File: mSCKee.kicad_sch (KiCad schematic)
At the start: 1 part

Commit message: chore: Reinit and readd RP2040 minimal circuit
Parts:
- removed U?: RP2040, Package_DFN_QFN:QFN-56-1EP_7x7mm_P0.4mm_EP3.2x3.2mm, symbol MCU_RaspberryPi:RP2040
- added C1, C17, C4: 10u, Capacitor_SMD:C_0805_2012Metric, symbol Device:C
- added C10, C8: 1u, Capacitor_SMD:C_0402_1005Metric, symbol Device:C
- added C11, C12, C13, C14, C15, C16, C5, C6, C7, C9: 100n, Capacitor_SMD:C_0402_1005Metric, symbol Device:C
- added C2, C3: 15p, Capacitor_SMD:C_0402_1005Metric, symbol Device:C
- added H1, H2, H3, H4: MountingHole, MountingHole:MountingHole_2.7mm_M2.5, symbol Mechanical:MountingHole
- added J1: USB_B_Micro, RP2040_minimal:USB_Micro-B_Amphenol_10103594-0001LF_Horizontal_modified, symbol Connector:USB_B_Micro
- added J2: Conn_01x02, Connector_PinHeader_2.54mm:PinHeader_1x02_P2.54mm_Vertical, symbol Connector_Generic:Conn_01x02
- added J3, J4: Conn_02x18_Odd_Even, Connector_PinHeader_2.54mm:PinHeader_2x18_P2.54mm_Vertical, symbol Connector_Generic:Conn_02x18_Odd_Even
- added R1, R5: 1k, Resistor_SMD:R_0402_1005Metric, symbol Device:R
- added R2: DNF, Resistor_SMD:R_0402_1005Metric, symbol Device:R
- added R3, R4: 27, Resistor_SMD:R_0402_1005Metric, symbol Device:R
- added U1: NCP1117-3.3_SOT223, Package_TO_SOT_SMD:SOT-223-3_TabPin2, symbol Regulator_Linear:NCP1117-3.3_SOT223
- added U2: W25Q128JVS, Package_SO:SOIC-8_5.23x5.23mm_P1.27mm, symbol Memory_Flash:W25Q128JVS
- added U3: RP2040, RP2040_minimal:RP2040-QFN-56, symbol MCU_RaspberryPi_RP2040:RP2040
- added Y1: ABM8-272-T3, Crystal:Crystal_SMD_3225-4Pin_3.2x2.5mm, symbol Device:Crystal_GND24
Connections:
- new net: R4.2, U3.46 (USB_DM)
- new net: R3.2, U3.47 (USB_DP)
- new net: C3.1, R5.2, Y1.3
- new net +1V1: C6.1, C7.1, C8.1, U3.23 (DVDD), U3.45 (VREG_VOUT), U3.50 (DVDD)
- new net +3V3: C10.1, C11.1, C12.1, C13.1, C14.1, C15.1, C16.1, C17.1, C4.1, C5.1, C9.1, J3.2 (Pin_2), R2.1, U1.2 (VO), U2.8 (VCC), U3.1 (IOVDD), U3.10 (IOVDD), U3.22 (IOVDD), U3.33 (IOVDD), U3.42 (IOVDD), U3.43 (ADC_AVDD), U3.44 (VREG_IN), U3.48 (USB_VDD), U3.49 (IOVDD)
- new net GND: C1.2, C10.2, C11.2, C12.2, C13.2, C14.2, C15.2, C16.2, C17.2, C2.2, C3.2, C4.2, C5.2, C6.2, C7.2, C8.2, C9.2, J1.5 (GND), J1.6 (Shield), J2.2 (Pin_2), J3.1 (Pin_1), J3.11 (Pin_11), J3.13 (Pin_13), J3.15 (Pin_15), J3.17 (Pin_17), J3.19 (Pin_19), J3.21 (Pin_21), J3.23 (Pin_23), J3.25 (Pin_25), J3.27 (Pin_27), J3.29 (Pin_29), J3.3 (Pin_3), J3.31 (Pin_31), J3.33 (Pin_33), J3.35 (Pin_35), J3.36 (Pin_36), J3.5 (Pin_5), J3.7 (Pin_7), J3.9 (Pin_9), J4.10 (Pin_10), J4.12 (Pin_12), J4.14 (Pin_14), J4.16 (Pin_16), J4.18 (Pin_18), J4.2 (Pin_2), J4.20 (Pin_20), J4.22 (Pin_22), J4.24 (Pin_24), J4.26 (Pin_26), J4.28 (Pin_28), J4.30 (Pin_30), J4.32 (Pin_32), J4.34 (Pin_34), J4.35 (Pin_35), J4.36 (Pin_36), J4.4 (Pin_4), J4.6 (Pin_6), J4.8 (Pin_8), U1.1 (GND), U2.4 (GND), U3.19 (TESTEN), U3.57 (GND), Y1.2, Y1.4
- new net GPIO0: J3.4 (Pin_4)
- new net GPIO1: J3.6 (Pin_6)
- new net GPIO10: J3.24 (Pin_24)
- new net GPIO11: J3.26 (Pin_26)
- new net GPIO12: J3.28 (Pin_28)
- new net GPIO13: J3.30 (Pin_30)
- new net GPIO14: J3.32 (Pin_32)
- new net GPIO15: J3.34 (Pin_34)
- new net GPIO16: J4.27 (Pin_27)
- new net GPIO17: J4.25 (Pin_25)
- new net GPIO18: J4.23 (Pin_23)
- new net GPIO19: J4.21 (Pin_21)
- new net GPIO2: J3.8 (Pin_8)
- new net GPIO20: J4.19 (Pin_19)
- new net GPIO21: J4.17 (Pin_17)
- new net GPIO22: J4.15 (Pin_15)
- new net GPIO23: J4.13 (Pin_13)
- new net GPIO24: J4.11 (Pin_11)
- new net GPIO25: J4.9 (Pin_9)
- new net GPIO26_ADC0: J4.7 (Pin_7)
- new net GPIO27_ADC1: J4.5 (Pin_5)
- new net GPIO28_ADC2: J4.3 (Pin_3)
- new net GPIO29_ADC3: J4.1 (Pin_1)
- new net GPIO3: J3.10 (Pin_10)
- new net GPIO4: J3.12 (Pin_12)
- new net GPIO5: J3.14 (Pin_14)
- new net GPIO6: J3.16 (Pin_16)
- new net GPIO7: J3.18 (Pin_18)
- new net GPIO8: J3.20 (Pin_20)
- new net GPIO9: J3.22 (Pin_22)
- new net QSPI_SCLK: U2.6 (CLK)
- new net QSPI_SD0: U2.5 (DI(IO0))
- new net QSPI_SD1: U2.2 (DO(IO1))
- new net QSPI_SD2: U2.3 (IO2)
- new net QSPI_SD3: U2.7 (IO3)
- new net QSPI_SS: R1.1, R2.2, U2.1 (~{CS})
- new net RUN: J4.29 (Pin_29)
- new net SWCLK: J4.33 (Pin_33)
- new net SWD: J4.31 (Pin_31)
- new net USB_D+: J1.3 (D+), R3.1
- new net USB_D-: J1.2 (D-), R4.1
- new net VBUS: C1.1, J1.1 (VBUS), U1.3 (VI)
- new net XIN: C2.1, U3.20 (XIN), Y1.1
- new net XOUT: R5.1, U3.21 (XOUT)
- new net ~{USB_BOOT}: J2.1 (Pin_1), R1.2
- no-connect marks 0 -> 1
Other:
- note added: "Crystal"
- note added: "Flash"
- note added: "IOs"
- note added: "Make sure C10 is close to pin 44 of RP2040"
- note added: "Make sure C8 is close to pin 45 of RP2040"
- note added: "Make sure R3 and R4 are close to RP2040"
- note added: "Power"

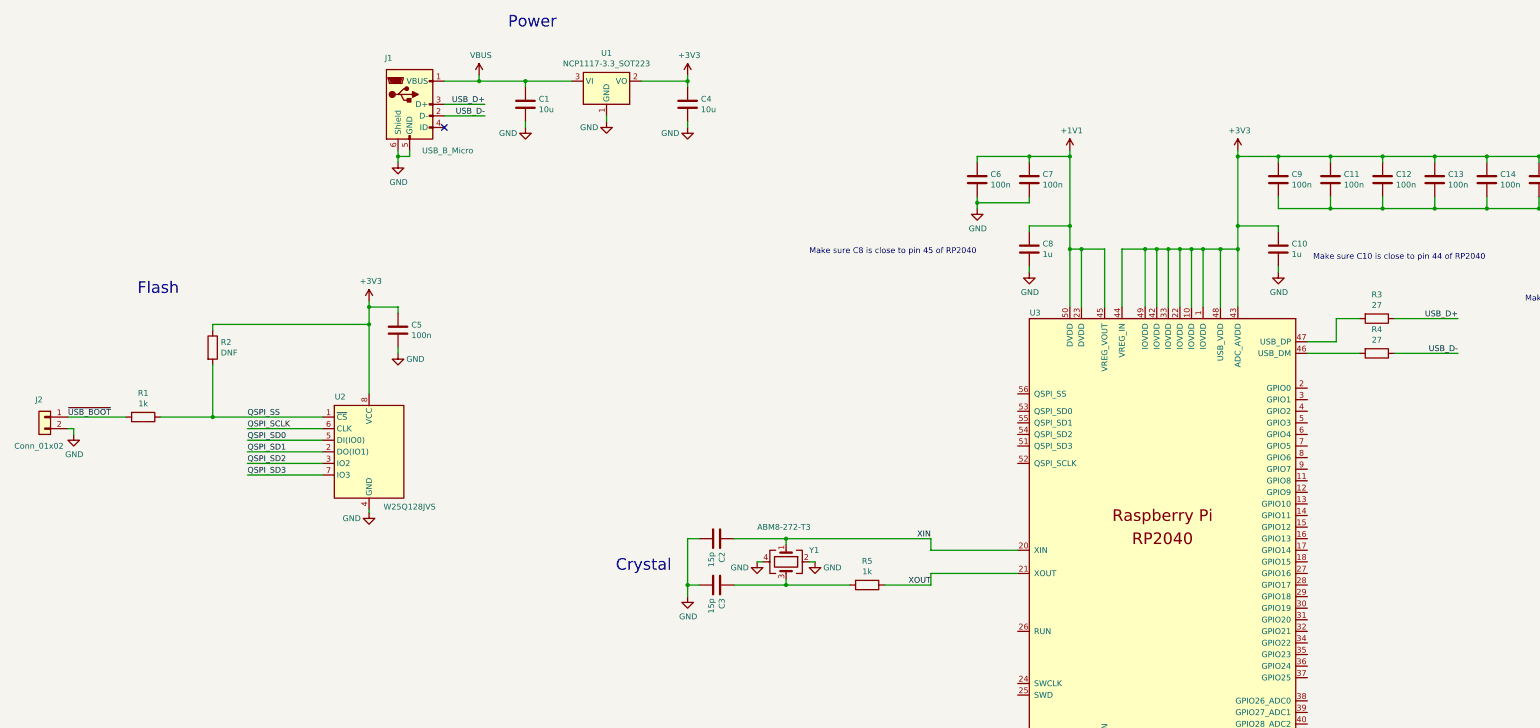
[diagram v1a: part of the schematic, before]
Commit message: feat(schematic): Connect crystal and flash chip to RP2040
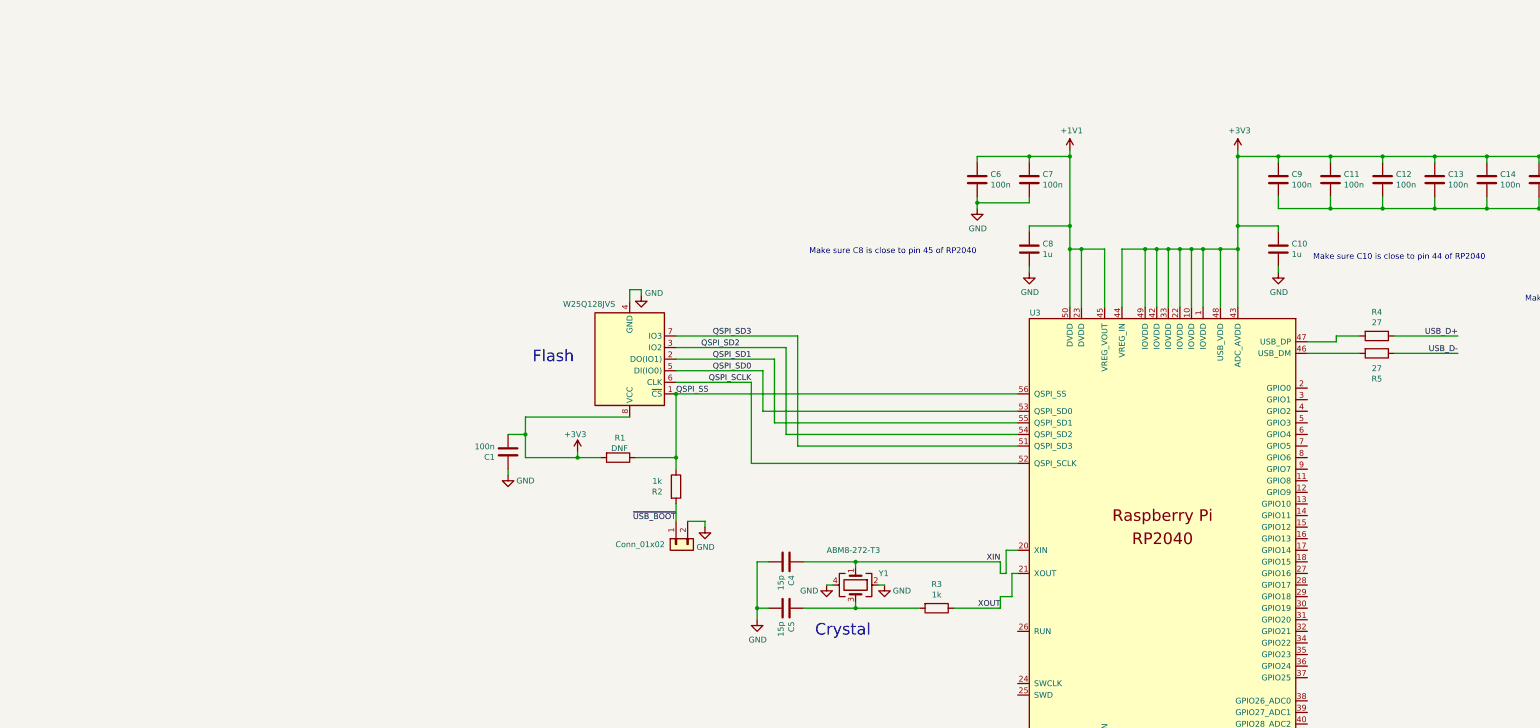
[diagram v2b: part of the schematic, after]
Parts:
- removed C1, C4: 10u, Capacitor_SMD:C_0805_2012Metric, symbol Device:C
- removed J1: USB_B_Micro, RP2040_minimal:USB_Micro-B_Amphenol_10103594-0001LF_Horizontal_modified, symbol Connector:USB_B_Micro
- removed U1: NCP1117-3.3_SOT223, Package_TO_SOT_SMD:SOT-223-3_TabPin2, symbol Regulator_Linear:NCP1117-3.3_SOT223
- removed U2: W25Q128JVS, Package_SO:SOIC-8_5.23x5.23mm_P1.27mm, symbol Memory_Flash:W25Q128JVS
- added U1: W25Q128JVS, W25Q128JVSIQ:SOIC127P790X216-8N, symbol library:W25Q128JVS
- C1: renamed from C5; symbol Device:C -> library:C
- C10, C11, C12, C13, C14, C15, C16, C17, C6, C7, C8, C9: symbol Device:C -> library:C
- C4: renamed from C2; symbol Device:C -> library:C
- C5: renamed from C3; symbol Device:C -> library:C
- H1, H2, H3, H4: symbol Mechanical:MountingHole -> library:MountingHole
- J2: symbol Connector_Generic:Conn_01x02 -> library:Conn_01x02
- J3, J4: symbol Connector_Generic:Conn_02x18_Odd_Even -> library:Conn_02x18_Odd_Even
- R1: renamed from R2; symbol Device:R -> library:R
- R2: renamed from R1; symbol Device:R -> library:R
- R3: renamed from R5; symbol Device:R -> library:R
- R4: renamed from R3; symbol Device:R -> library:R
- R5: renamed from R4; symbol Device:R -> library:R
- U3: footprint RP2040_minimal:RP2040-QFN-56 -> Package_DFN_QFN:QFN-56-1EP_7x7mm_P0.4mm_EP3.2x3.2mm; symbol MCU_RaspberryPi_RP2040:RP2040 -> library:RP2040
- Y1: symbol Device:Crystal_GND24 -> library:Crystal_GND24
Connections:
- net +3V3: now also C1.2, R1.2, U1.8 (VCC); no longer C1.1, R1.1
- net GND: now also C1.1, U1.4 (GND); no longer C1.2
- net QSPI_SCLK: now also U3.52 (QSPI_SCLK), U1.6 (CLK)
- net QSPI_SD0: now also U3.53 (QSPI_SD0), U1.5 (DI(IO0))
- net QSPI_SD1: now also U3.55 (QSPI_SD1), U1.2 (DO(IO1))
- net QSPI_SD2: now also U3.54 (QSPI_SD2), U1.3 (IO2)
- net QSPI_SD3: now also U3.51 (QSPI_SD3), U1.7 (IO3)
- net QSPI_SS: now also R1.1, U3.56 (QSPI_SS), U1.1 (~{CS}); no longer R1.2
- no-connect marks 1 -> 0
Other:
- note removed: "Power"
- moved on the sheet: C1, C4, C5, R1, R2, R3, R4, Y1

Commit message: feat(schematic): Wire up USB-C receptacle
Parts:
- added C2, C3: 10u, Capacitor_SMD:C_0805_2012Metric, symbol Device:C
- added J5: USB_C_Receptacle_USB2.0_14P, symbol Connector:USB_C_Receptacle_USB2.0_14P
- added R6, R7: 5.1k, symbol library:R
- added TP1, TP2: TestPoint, symbol Connector:TestPoint
- added U2: NCP1117-3.3_SOT223, Package_TO_SOT_SMD:SOT-223-3_TabPin2, symbol Regulator_Linear:NCP1117-3.3_SOT223
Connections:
- net +3V3: now also C3.1, U2.2 (VO)
- net GND: now also C2.2, C3.2, J5.A1 (GND), J5.A12 (GND), J5.B1 (GND), J5.B12 (GND), J5.S1 (SHIELD), R6.1, R7.1, TP2.1, U2.1 (GND)
- net USB_D+: now also J5.A6 (D+), J5.B6 (D+)
- net USB_D-: now also J5.A7 (D-), J5.B7 (D-)
- net +1V1: no longer names the net of C6.1, C7.1, C8.1, U3.23 (DVDD), U3.45 (VREG_VOUT), U3.50 (DVDD)
- new net: C2.1, J5.A4 (VBUS), J5.A9 (VBUS), J5.B4 (VBUS), J5.B9 (VBUS), TP1.1, U2.3 (VI)
- new net: J5.B5 (CC2), R6.2
- new net: J5.A5 (CC1), R7.2
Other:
- note added: "Power"
- title: (none) -> mSCKee - Split Keyboard
- moved on the sheet: C11, C12, C13, C14, C15, C16, C17, C4, C5, C9, J3, J4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

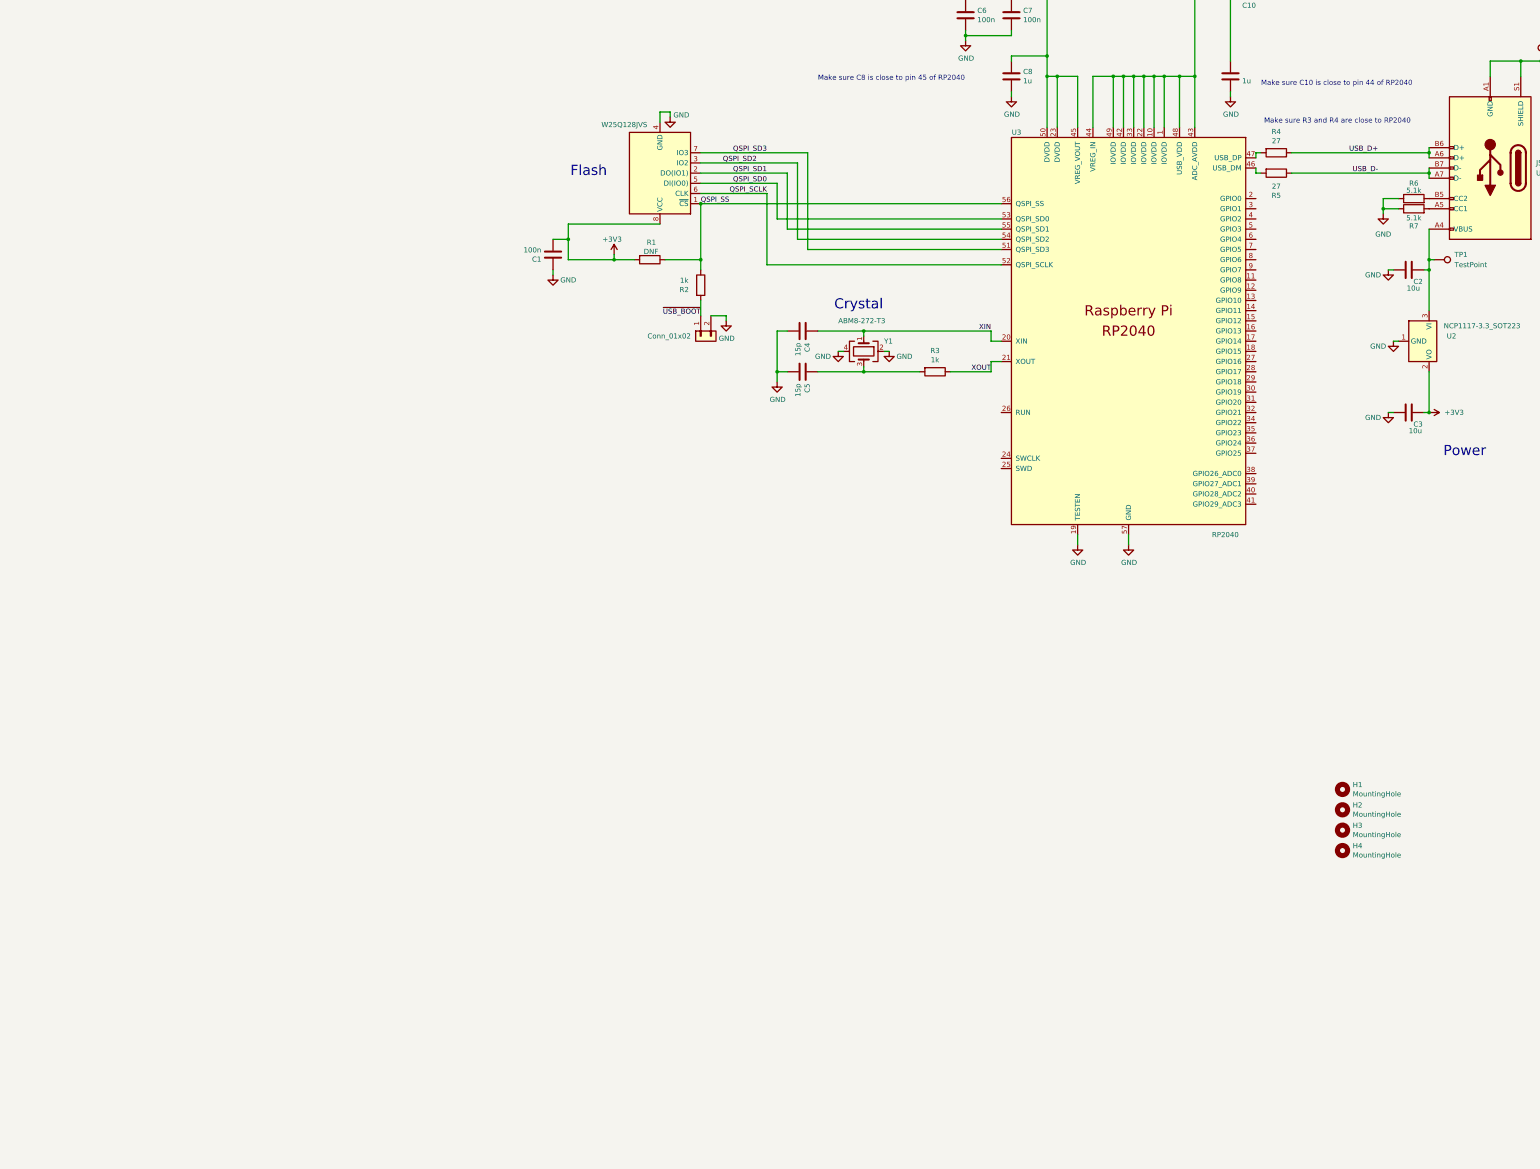
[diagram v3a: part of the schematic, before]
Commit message: feat(schematic): Add GPIO connection labels and an LED to one
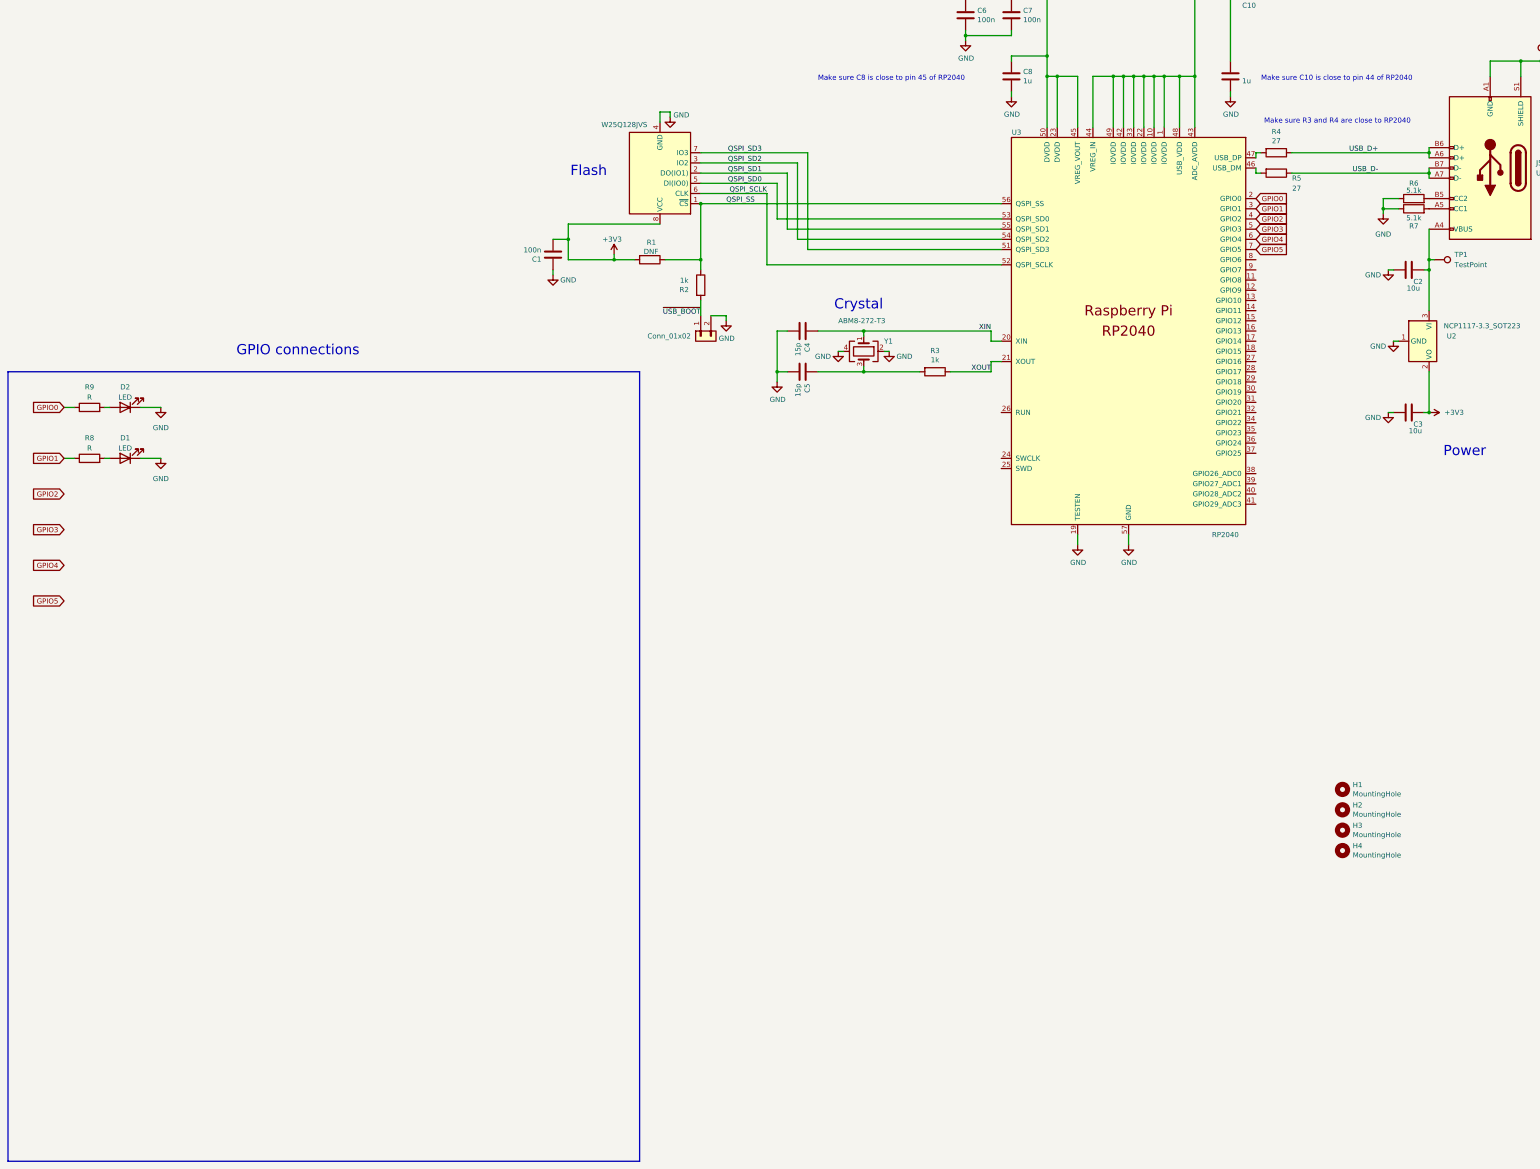
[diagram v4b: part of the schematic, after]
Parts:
- added D1, D2: LED, symbol Device:LED
- added R8, R9: R, symbol library:R
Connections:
- net GND: now also D1.1 (K), D2.1 (K)
- net GPIO0: now also U3.2 (GPIO0), R9.1
- net GPIO1: now also U3.3 (GPIO1), R8.1
- net GPIO2: now also U3.4 (GPIO2)
- net GPIO3: now also U3.5 (GPIO3)
- net GPIO4: now also U3.6 (GPIO4)
- net GPIO5: now also U3.7 (GPIO5)
- new net: D1.2 (A), R8.2
- new net: D2.2 (A), R9.2
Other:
- note added: "GPIO connections"

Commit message: misc: Add keep QSPI conn short
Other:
- note added: "keep QSPI conections short"
- moved on the sheet: C1, R1, R2

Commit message: feat: Add TRRS receptacle and split sheets into master & slave side
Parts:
- removed C1, C11, C12, C13, C14, C15, C16, C6, C7, C9: 100n, Capacitor_SMD:C_0402_1005Metric, symbol library:C
- removed C10, C8: 1u, Capacitor_SMD:C_0402_1005Metric, symbol library:C
- removed C17: 10u, Capacitor_SMD:C_0805_2012Metric, symbol library:C
- removed C2, C3: 10u, Capacitor_SMD:C_0805_2012Metric, symbol Device:C
- removed C4, C5: 15p, Capacitor_SMD:C_0402_1005Metric, symbol library:C
- removed D1, D2: LED, symbol Device:LED
- removed H1, H2, H3, H4: MountingHole, MountingHole:MountingHole_2.7mm_M2.5, symbol library:MountingHole
- removed J2: Conn_01x02, Connector_PinHeader_2.54mm:PinHeader_1x02_P2.54mm_Vertical, symbol library:Conn_01x02
- removed J3, J4: Conn_02x18_Odd_Even, Connector_PinHeader_2.54mm:PinHeader_2x18_P2.54mm_Vertical, symbol library:Conn_02x18_Odd_Even
- removed J5: USB_C_Receptacle_USB2.0_14P, symbol Connector:USB_C_Receptacle_USB2.0_14P
- removed R1: DNF, Resistor_SMD:R_0402_1005Metric, symbol library:R
- removed R2, R3: 1k, Resistor_SMD:R_0402_1005Metric, symbol library:R
- removed R4, R5: 27, Resistor_SMD:R_0402_1005Metric, symbol library:R
- removed R6, R7: 5.1k, symbol library:R
- removed R8, R9: R, symbol library:R
- removed TP1, TP2: TestPoint, symbol Connector:TestPoint
- removed U1: W25Q128JVS, W25Q128JVSIQ:SOIC127P790X216-8N, symbol library:W25Q128JVS
- removed U2: NCP1117-3.3_SOT223, Package_TO_SOT_SMD:SOT-223-3_TabPin2, symbol Regulator_Linear:NCP1117-3.3_SOT223
- removed U3: RP2040, Package_DFN_QFN:QFN-56-1EP_7x7mm_P0.4mm_EP3.2x3.2mm, symbol library:RP2040
- removed Y1: ABM8-272-T3, Crystal:Crystal_SMD_3225-4Pin_3.2x2.5mm, symbol library:Crystal_GND24
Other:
- added sheet master_side (master_side.kicad_sch)
- added sheet slave_side (slave_side.kicad_sch)
- note removed: "Crystal"
- note removed: "Flash"
- note removed: "GPIO connections"
- note removed: "IOs"
- note removed: "Make sure C10 is close to pin 44 of RP2040"
- note removed: "Make sure C8 is close to pin 45 of RP2040"
- note removed: "Make sure R3 and R4 are close to RP2040"
- note removed: "Power"
- note removed: "keep QSPI conections short"
- title: mSCKee - Split Keyboard -> mSCKee - master side

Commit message: Add TRRS connector, rotary encoder, ambient light sensor
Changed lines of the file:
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@@
 	)
 	(sheet
-		(at 22.86 148.59)
+		(at 307.34 135.89)
 		(size 262.89 185.42)
 		(exclude_from_sim no)
@@
 		)
 		(property "Sheetname" "slave_side"
-			(at 22.86 147.8784 0)
+			(at 307.34 135.1784 0)
 			(effects
 				(font
@@
 		)
 		(property "Sheetfile" "slave_side.kicad_sch"
-			(at 22.86 334.5946 0)
+			(at 307.34 321.8946 0)
 			(effects
 				(font
@@
 	)
 	(sheet
-		(at 306.07 148.59)
+		(at 21.59 135.89)
 		(size 262.89 185.42)
 		(exclude_from_sim no)
@@
 		)
 		(property "Sheetname" "master_side"
-			(at 306.07 147.8784 0)
+			(at 21.59 135.1784 0)
 			(effects
 				(font
@@
 		)
 		(property "Sheetfile" "master_side.kicad_sch"
-			(at 306.07 334.5946 0)
+			(at 21.59 321.8946 0)
 			(effects
 				(font
